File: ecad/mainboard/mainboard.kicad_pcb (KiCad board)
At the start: 2 copper layers, 31 parts, among them J1 Dot Matrix Side A (M), J2 Dot Matrix Side B (M), J3 Dot Matrix Side A (F), J4 Dot Matrix Side B (F), J5 ESP32C3 Super Mini Left, J6 ESP32C3 Super Mini Right, J8 IO Expander Module - Left, J9 IO Expander Module - Right, SW1 Left Button, SW2 Right Button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

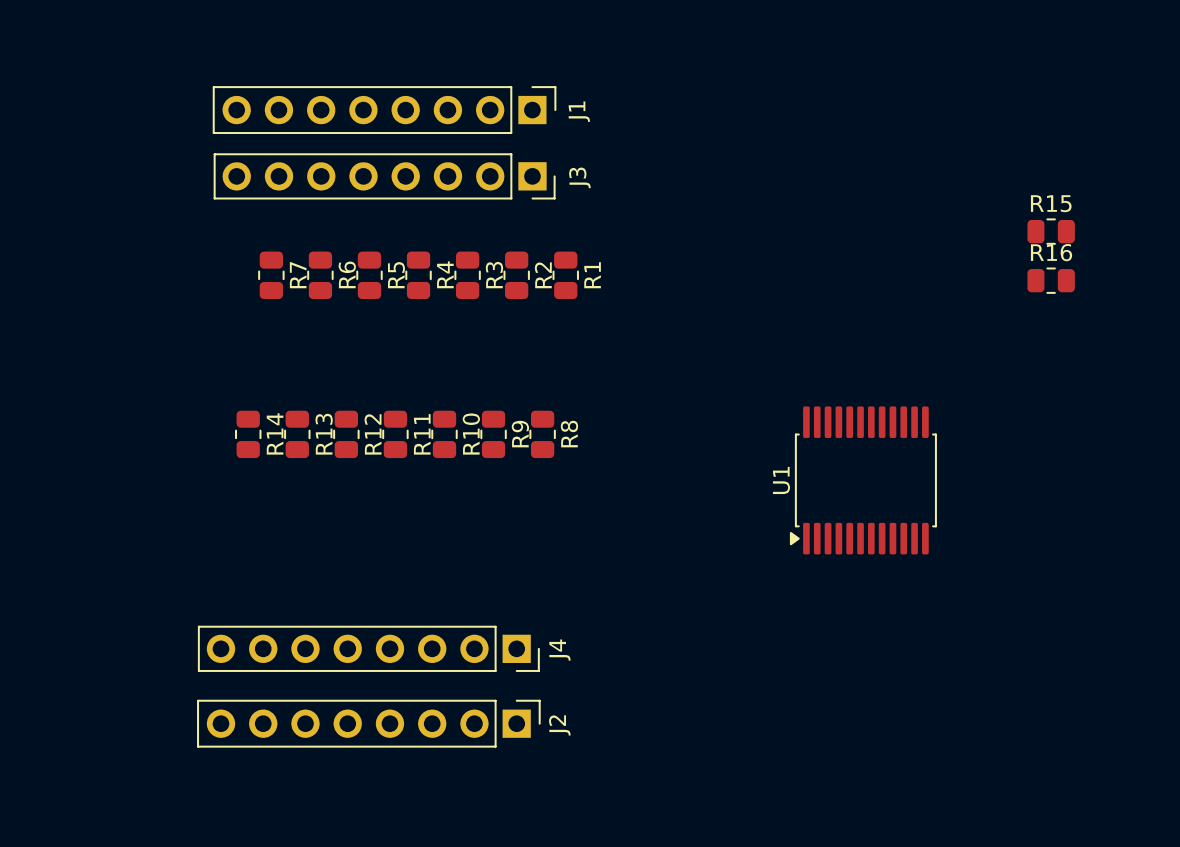
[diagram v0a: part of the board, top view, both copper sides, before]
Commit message: position dot matrix headers
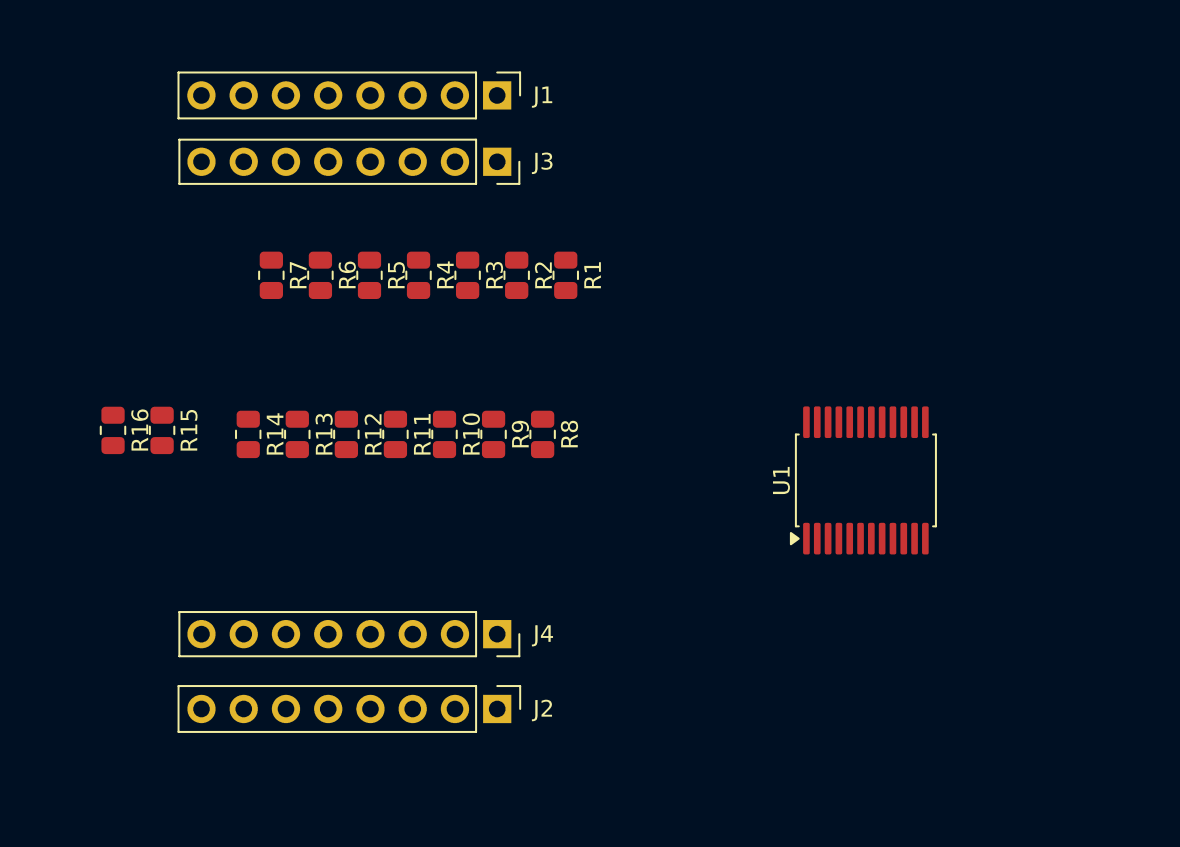
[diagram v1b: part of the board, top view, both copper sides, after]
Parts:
- moved R16 57.1 mm to (97.5, 80.4), turned to -90 degrees
- moved R15 54.8 mm to (100.5, 80.4), turned to -90 degrees
- moved J1 2.29 mm to (120.6, 60.3)
- moved J3 2.29 mm to (120.7, 64.3)
- moved J2 1.47 mm to (120.6, 97.2)
- moved J4 1.47 mm to (120.6, 92.7)
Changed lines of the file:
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@@
 	(footprint "Resistor_SMD:R_0805_2012Metric"
 		(layer "F.Cu")
-		(at 153.9525 71.41)
+		(at 97.55 80.4125 -90)
 		(descr "Resistor SMD 0805 (2012 Metric), square (rectangular) end terminal, IPC-7351 nominal, (Body size source: IPC-SM-782 page 72, https://www.pcb-3d.com/wordpress/wp-content/uploads/ipc-sm-782a_amendment_1_and_2.pdf)")
 		(tags "resistor")
 		(property "Reference" "R16"
-			(at 0 -1.65 0)
+			(at 0 -1.65 90)
 			(layer "F.SilkS")
 			(effects
@@
 		)
 		(property "Value" "150"
-			(at 0 1.65 0)
+			(at 0 1.65 90)
 			(layer "F.Fab")
 			(effects
@@
 		)
 		(property "Datasheet" ""
-			(at 0 0 0)
+			(at 0 0 90)
 			(layer "F.Fab")
 			(hide yes)
@@
 		)
 		(property "Description" "Resistor, US symbol"
-			(at 0 0 0)
+			(at 0 0 90)
 			(layer "F.Fab")
 			(hide yes)
@@
 		)
 		(property "KiLib_Generator" "SMD_2terminal_chip_molded"
-			(at 0 0 0)
+			(at 0 0 90)
 			(layer "F.SilkS")
 			(hide yes)
@@
 		(duplicate_pad_numbers_are_jumpers no)
 		(fp_line
-			(start -0.227064 -0.735)
-			(end 0.227064 -0.735)
+			(start -0.227064 0.735)
+			(end 0.227064 0.735)
 			(stroke
 				(width 0.12)
@@
 		)
 		(fp_line
-			(start -0.227064 0.735)
-			(end 0.227064 0.735)
+			(start -0.227064 -0.735)
+			(end 0.227064 -0.735)
 			(stroke
 				(width 0.12)
@@
 		)
 		(fp_text user "${REFERENCE}"
-			(at 0 0 0)
+			(at 0 0 90)
 			(layer "F.Fab")
 			(effects
@@
 		)
 		(pad "1" smd roundrect
-			(at -0.9125 0)
+			(at -0.9125 0 270)
 			(size 1.025 1.4)
 			(layers "F.Cu" "F.Mask" "F.Paste")
@@
 		)
 		(pad "2" smd roundrect
-			(at 0.9125 0)
+			(at 0.9125 0 270)
 			(size 1.025 1.4)
 			(layers "F.Cu" "F.Mask" "F.Paste")
@@
 	(footprint "Connector_PinSocket_2.54mm:PinSocket_1x08_P2.54mm_Vertical"
 		(layer "F.Cu")
-		(at 122.77 65.14 -90)
+		(at 120.65 64.262 -90)
 		(descr "Through hole straight socket strip, 1x08, 2.54mm pitch, single row (from Kicad 4.0.7), script generated")
 		(tags "Through hole socket strip THT 1x08 2.54mm single row")
 		(property "Reference" "J3"
-			(at 0 -2.76 90)
+			(at 0 -2.7939 180)
 			(layer "F.SilkS")
 			(effects
@@
 	(footprint "Connector_PinHeader_2.54mm:PinHeader_1x08_P2.54mm_Vertical"
 		(layer "F.Cu")
-		(at 122.766 61.152 -90)
+		(at 120.646 60.274 -90)
 		(descr "Through hole straight pin header, 1x08, 2.54mm pitch, single row")
 		(tags "Through hole pin header THT 1x08 2.54mm single row")
 		(property "Reference" "J1"
-			(at 0 -2.72 90)
+			(at 0 -2.7979 180)
 			(layer "F.SilkS")
 			(effects
@@
 	(footprint "Resistor_SMD:R_0805_2012Metric"
 		(layer "F.Cu")
-		(at 153.9525 68.46)
+		(at 100.5 80.4125 -90)
 		(descr "Resistor SMD 0805 (2012 Metric), square (rectangular) end terminal, IPC-7351 nominal, (Body size source: IPC-SM-782 page 72, https://www.pcb-3d.com/wordpress/wp-content/uploads/ipc-sm-782a_amendment_1_and_2.pdf)")
 		(tags "resistor")
 		(property "Reference" "R15"
-			(at 0 -1.65 0)
+			(at 0 -1.65 90)
 			(layer "F.SilkS")
 			(effects
@@
 		)
 		(property "Value" "150"
-			(at 0 1.65 0)
+			(at 0 1.65 90)
 			(layer "F.Fab")
 			(effects
@@
 		)
 		(property "Datasheet" ""
-			(at 0 0 0)
+			(at 0 0 90)
 			(layer "F.Fab")
 			(hide yes)
@@
 		)
 		(property "Description" "Resistor, US symbol"
-			(at 0 0 0)
+			(at 0 0 90)
 			(layer "F.Fab")
 			(hide yes)
@@
 		)
 		(property "KiLib_Generator" "SMD_2terminal_chip_molded"
-			(at 0 0 0)
+			(at 0 0 90)
 			(layer "F.SilkS")
 			(hide yes)
@@
 		(duplicate_pad_numbers_are_jumpers no)
 		(fp_line
-			(start -0.227064 -0.735)
-			(end 0.227064 -0.735)
+			(start -0.227064 0.735)
+			(end 0.227064 0.735)
 			(stroke
 				(width 0.12)
@@
 		)
 		(fp_line
-			(start -0.227064 0.735)
-			(end 0.227064 0.735)
+			(start -0.227064 -0.735)
+			(end 0.227064 -0.735)
 			(stroke
 				(width 0.12)
@@
 		)
 		(fp_text user "${REFERENCE}"
-			(at 0 0 0)
+			(at 0 0 90)
 			(layer "F.Fab")
 			(effects
@@
 		)
 		(pad "1" smd roundrect
-			(at -0.9125 0)
+			(at -0.9125 0 270)
 			(size 1.025 1.4)
 			(layers "F.Cu" "F.Mask" "F.Paste")
@@
 		)
 		(pad "2" smd roundrect
-			(at 0.9125 0)
+			(at 0.9125 0 270)
 			(size 1.025 1.4)
 			(layers "F.Cu" "F.Mask" "F.Paste")
@@
 	(footprint "Connector_PinSocket_2.54mm:PinSocket_1x08_P2.54mm_Vertical"
 		(layer "F.Cu")
-		(at 121.822 93.546 -90)
+		(at 120.6499 92.662 -90)
 		(descr "Through hole straight socket strip, 1x08, 2.54mm pitch, single row (from Kicad 4.0.7), script generated")
 		(tags "Through hole socket strip THT 1x08 2.54mm single row")
 		(property "Reference" "J4"
-			(at 0 -2.5 90)
+			(at 0 -2.794 180)
 			(layer "F.SilkS")
 			(effects
@@
 	(footprint "Connector_PinHeader_2.54mm:PinHeader_1x08_P2.54mm_Vertical"
 		(layer "F.Cu")
-		(at 121.822 98.046 -90)
+		(at 120.6499 97.162 -90)
 		(descr "Through hole straight pin header, 1x08, 2.54mm pitch, single row")
 		(tags "Through hole pin header THT 1x08 2.54mm single row")
 		(property "Reference" "J2"
-			(at 0 -2.5 90)
+			(at -0.002 -2.794 180)
 			(layer "F.SilkS")
 			(effects
@@
 		)
 	)
-	(dimension
-		(type orthogonal)
-		(layer "F.Cu")
-		(pts
-			(xy 104.99 65.14) (xy 104.042 93.546)
-		)
-		(height -5.588)
-		(orientation 1)
-		(format
-			(prefix "")
-			(suffix "")
-			(units 2)
-			(units_format 0)
-			(precision 4)
-			(suppress_zeroes yes)
-		)
-		(style
-			(thickness 0.2)
-			(arrow_length 1.27)
-			(text_position_mode 0)
-			(arrow_direction outward)
-			(extension_height 0.58642)
-			(extension_offset 0.5)
-			(keep_text_aligned yes)
-		)
-		(gr_text "28.406"
-			(at 97.602 79.343 90)
-			(layer "F.Cu")
-			(effects
-				(font
-					(size 1.5 1.5)
-					(thickness 0.3)
-				)
-			)
-		)
-	)
 	(group ""
-		(members "88ea9624-9b86-4507-a7a7-213c95ab365b" "8b98eaf7-5473-41b6-aa93-01c7dc8ed6a1"
-			"f0d95bce-4ad9-442f-a969-cd5bc7fa89f9"
+		(members "3b147e6b-49a4-4ee5-9ea5-e08daca15c0e" "4d2525f8-8133-4ff4-b847-ab6b40174733"
+			"79e48fc6-7967-4f1b-bbad-1cf8d092823a" "bbf46b6e-9964-4f9a-8dc1-b9d27fc4320c"
 		)
 	)
-	(group ""
-		(members "79e48fc6-7967-4f1b-bbad-1cf8d092823a" "bbf46b6e-9964-4f9a-8dc1-b9d27fc4320c")
-	)
-	(group ""
-		(members "3b147e6b-49a4-4ee5-9ea5-e08daca15c0e" "4d2525f8-8133-4ff4-b847-ab6b40174733")
-	)
 	(embedded_fonts no)

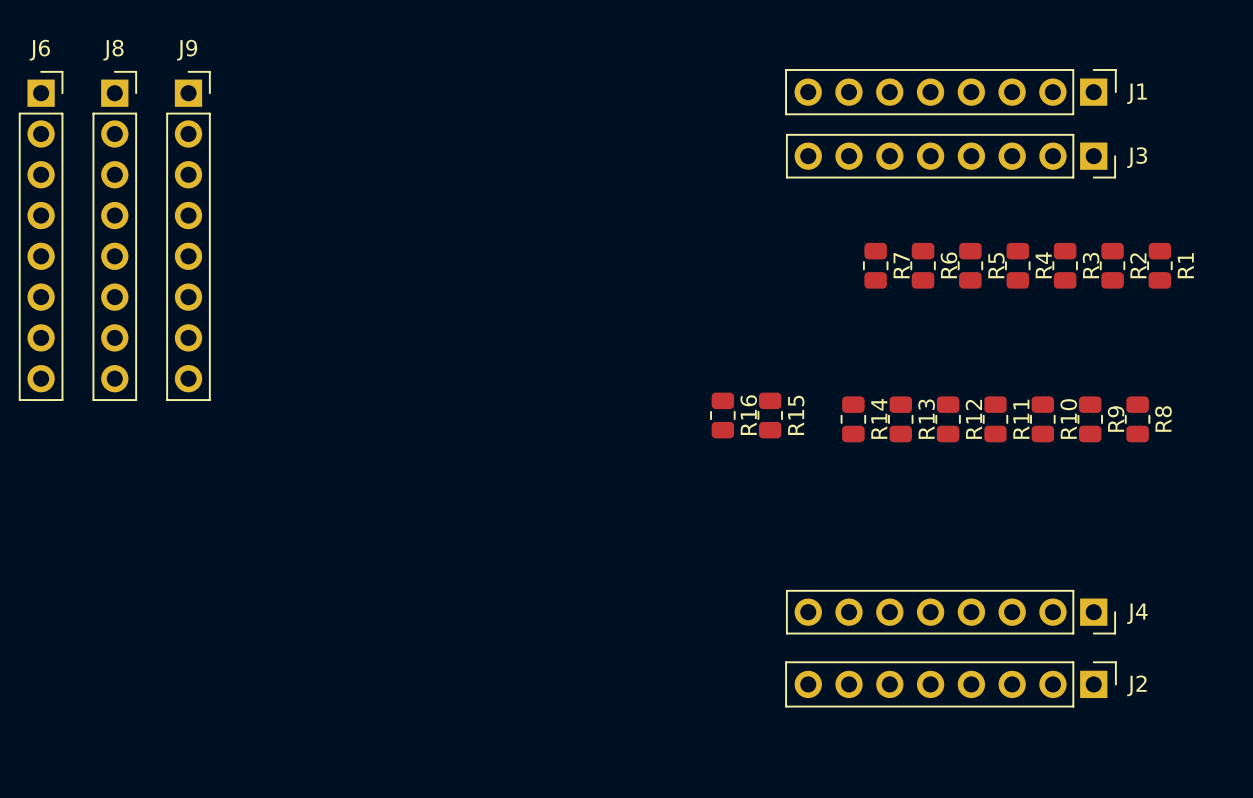
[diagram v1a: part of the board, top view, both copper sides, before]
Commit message: update pin headers for dot matrix
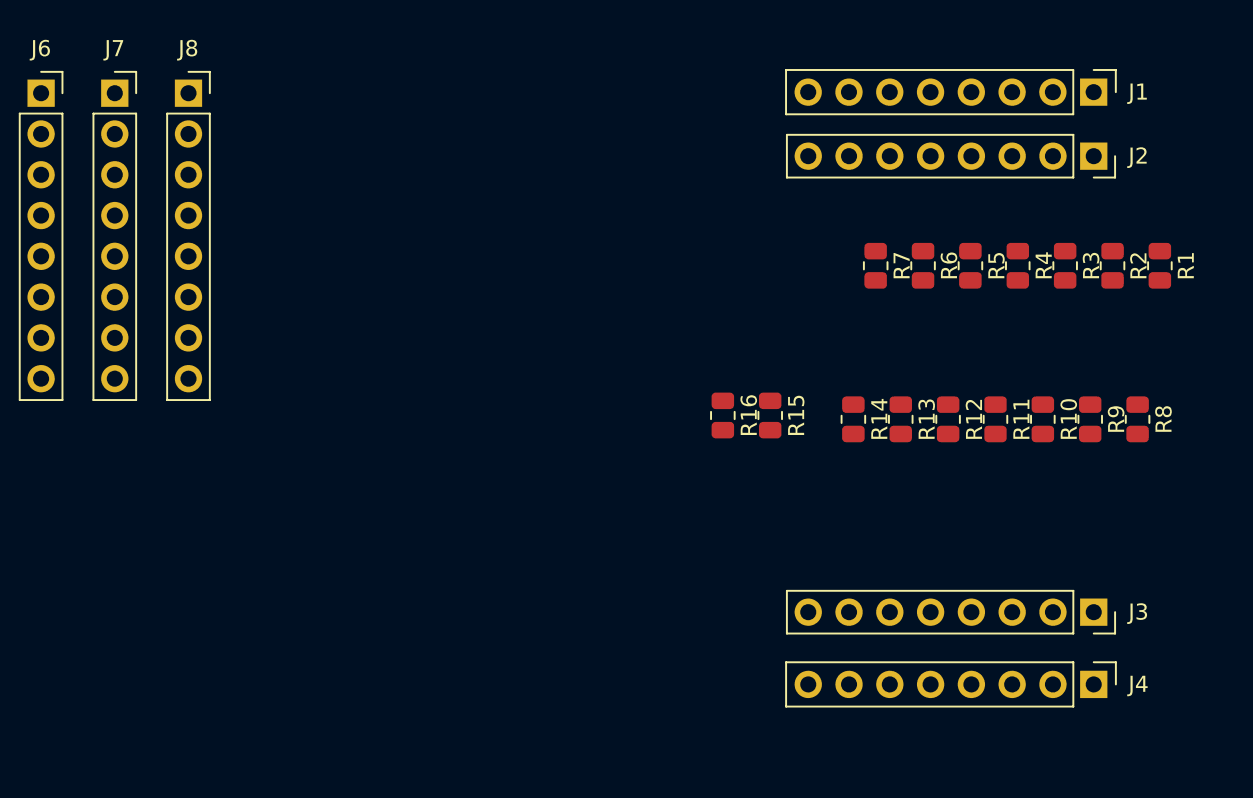
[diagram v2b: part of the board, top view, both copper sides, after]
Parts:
- renumbered J3 to J2, J4 to J3, J2 to J4, J8 to J7, J9 to J8
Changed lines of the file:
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@@
 		(descr "Through hole straight socket strip, 1x08, 2.54mm pitch, single row (from Kicad 4.0.7), script generated")
 		(tags "Through hole socket strip THT 1x08 2.54mm single row")
-		(property "Reference" "J3"
+		(property "Reference" "J2"
 			(at 0 -2.7939 180)
 			(layer "F.SilkS")
@@
 		(descr "Through hole straight socket strip, 1x08, 2.54mm pitch, single row (from Kicad 4.0.7), script generated")
 		(tags "Through hole socket strip THT 1x08 2.54mm single row")
-		(property "Reference" "J8"
+		(property "Reference" "J7"
 			(at 0 -2.77 0)
 			(layer "F.SilkS")
@@
 		(descr "Through hole straight socket strip, 1x08, 2.54mm pitch, single row (from Kicad 4.0.7), script generated")
 		(tags "Through hole socket strip THT 1x08 2.54mm single row")
-		(property "Reference" "J4"
+		(property "Reference" "J3"
 			(at 0 -2.794 180)
 			(layer "F.SilkS")
@@
 		(descr "Through hole straight pin header, 1x08, 2.54mm pitch, single row")
 		(tags "Through hole pin header THT 1x08 2.54mm single row")
-		(property "Reference" "J2"
+		(property "Reference" "J4"
 			(at -0.002 -2.794 180)
 			(layer "F.SilkS")
@@
 		(descr "Through hole straight socket strip, 1x08, 2.54mm pitch, single row (from Kicad 4.0.7), script generated")
 		(tags "Through hole socket strip THT 1x08 2.54mm single row")
-		(property "Reference" "J9"
+		(property "Reference" "J8"
 			(at 0 -2.77 0)
 			(layer "F.SilkS")

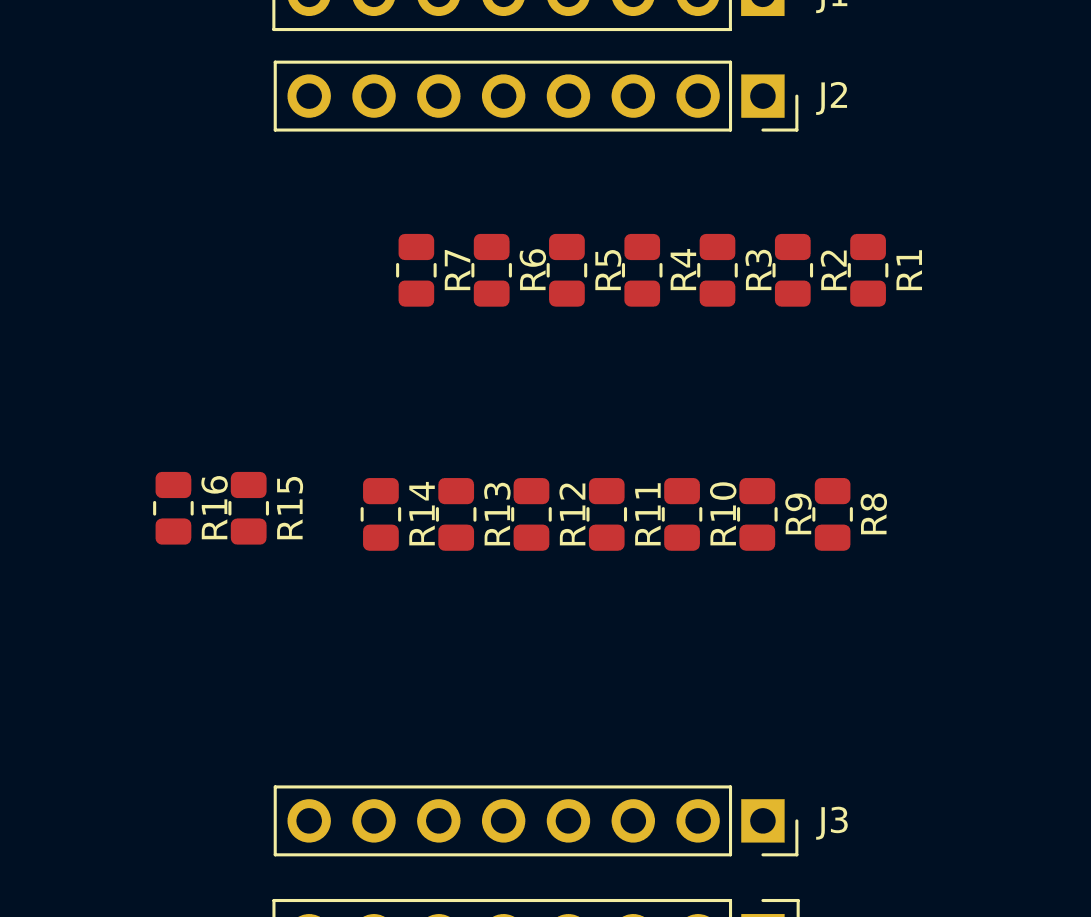
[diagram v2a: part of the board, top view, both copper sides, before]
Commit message: place resistors for the dot matrix
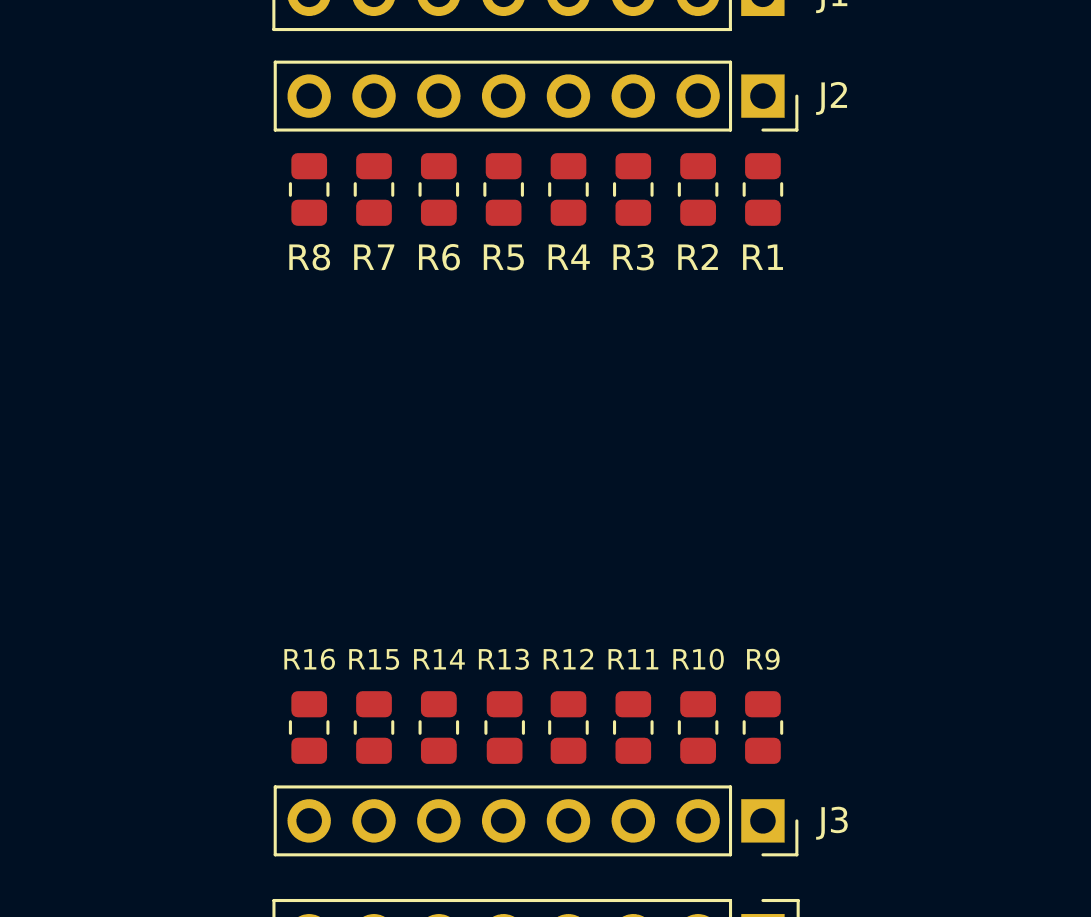
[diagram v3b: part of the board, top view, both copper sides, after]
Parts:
- moved R8 24.1 mm to (102.9, 67.9)
- moved R16 10.1 mm to (102.9, 89.0), turned to 90 degrees
- moved R15 9.90 mm to (105.4, 89.0), turned to 90 degrees
- moved R14 8.65 mm to (108.0, 89.0), turned to 90 degrees
- moved R13 8.56 mm to (110.5, 89.0), turned to 90 degrees
- moved R12 8.48 mm to (113.0, 89.0), turned to 90 degrees
- moved R11 8.42 mm to (115.6, 89.0), turned to 90 degrees
- moved R10 8.37 mm to (118.1, 89.0), turned to 90 degrees
- moved R9 8.35 mm to (120.7, 89.0), turned to 90 degrees
- moved R1 5.20 mm to (120.7, 67.9)
- moved R2 4.88 mm to (118.1, 67.9)
- moved R3 4.57 mm to (115.6, 67.9)
- moved R4 4.29 mm to (113.0, 67.9)
- moved R5 4.02 mm to (110.5, 67.9)
- moved R6 3.78 mm to (108.0, 67.9)
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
